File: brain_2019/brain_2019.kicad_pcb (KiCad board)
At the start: 2 copper layers, 54 x 50 mm, 60 parts, among them J1 CocobotCAN, J2 CocobotCAN, J3 JST_PH_S6B-PH-SM4-TB_06x2.00m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, J4 JST_PH_S2B-PH-SM4-TB_02x2.00m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, J5 Conn_01x02, J6 Conn_01x04, J7 JST_PH_S4B-PH-SM4-TB_04x2.00m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, J8 JST_PH_S4B-PH-SM4-TB_04x2.00m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, J9 JST_PH_S2B-PH-SM4-TB_02x2.00m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, U1 MAX3051ESA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

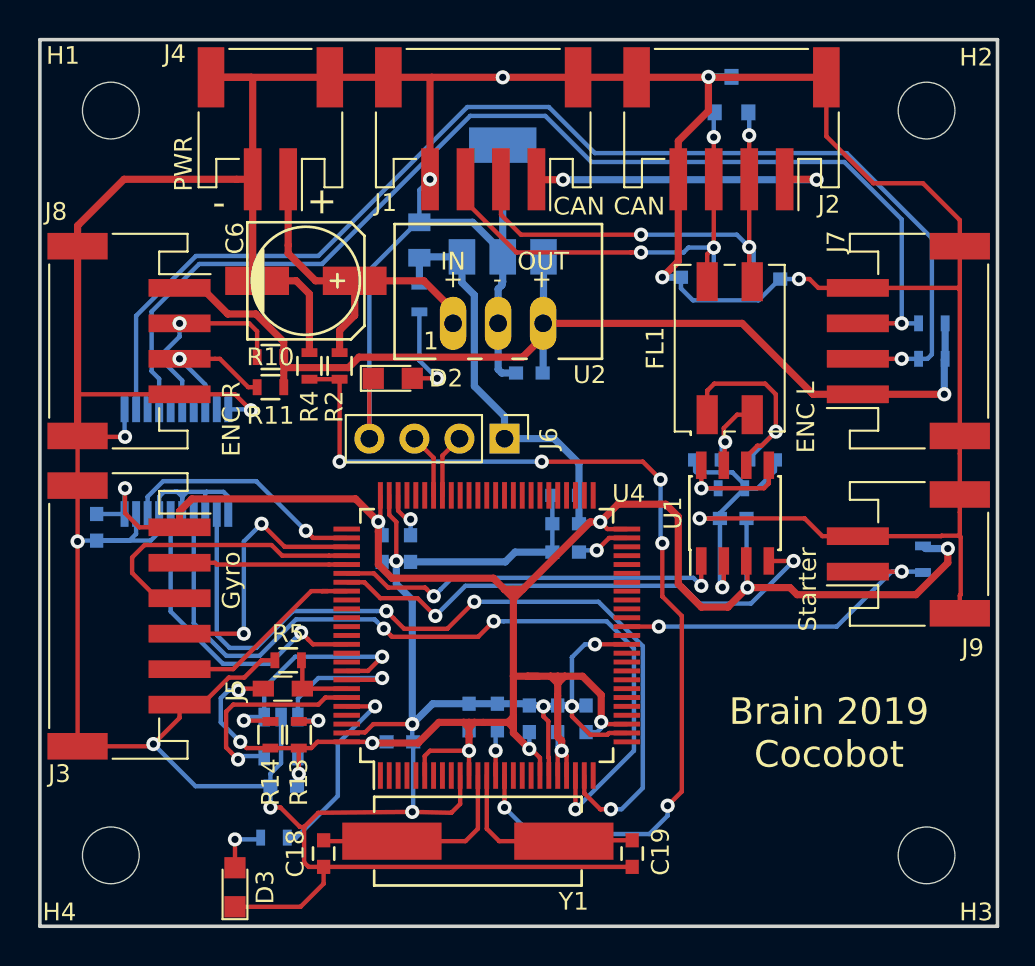
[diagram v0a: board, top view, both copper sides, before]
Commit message: Update brain 2019 with new CAN connector
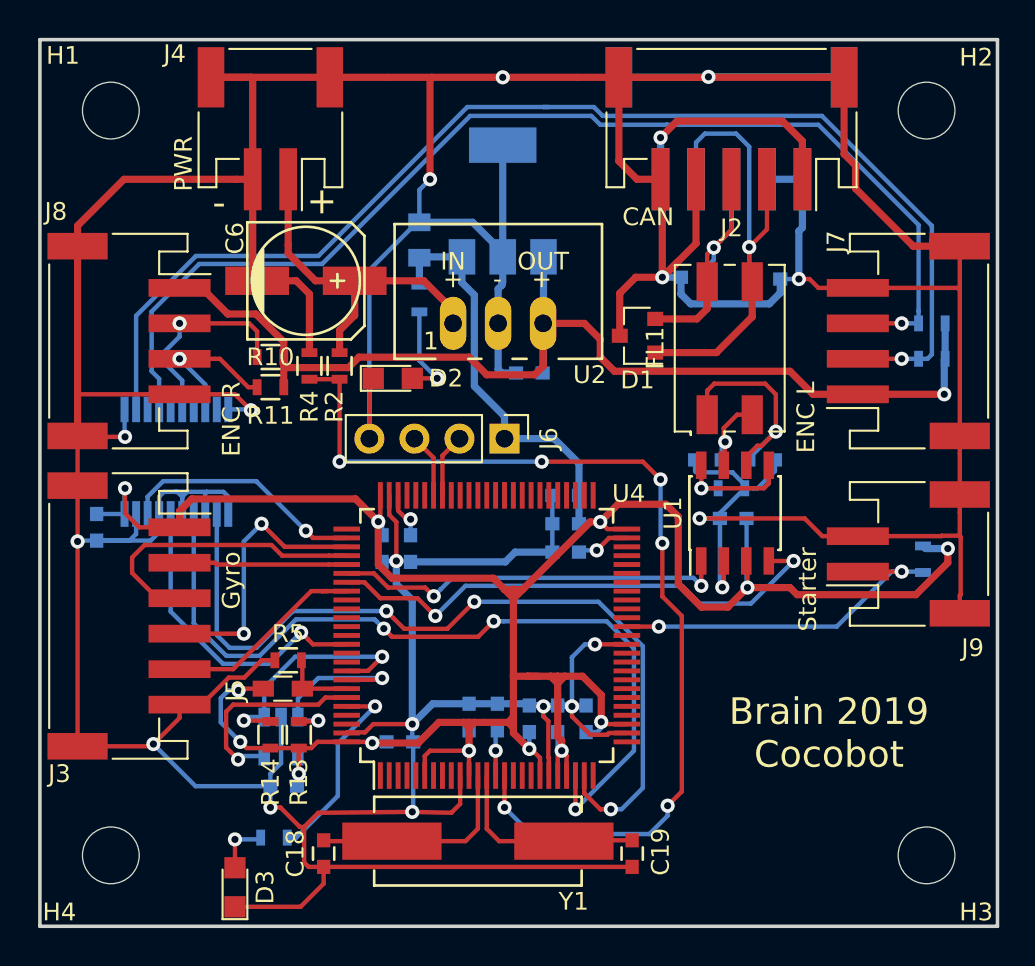
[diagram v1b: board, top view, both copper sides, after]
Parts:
- D1: moved to F.Cu
- J1: footprint espitall:JST_PH_S4B-PH-SM4-TB_04x2.00mm_Angled -> espitall:JST_PH_S5B-PH-SM4-TB_05x2.00mm_Angled; moved to B.Cu
- J2: footprint espitall:JST_PH_S4B-PH-SM4-TB_04x2.00mm_Angled -> espitall:JST_PH_S5B-PH-SM4-TB_05x2.00mm_Angled
- moved D1 14.6 mm to (83.7, 66.7), turned to 180 degrees
- moved J1 14.0 mm to (89.0, 55.0), turned to 0 degrees
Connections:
- H1 pad 1: Net-(H1-Pad1) -> (no net)
- H2 pad 1: Net-(H2-Pad1) -> (no net)
- H3 pad 1: Net-(H3-Pad1) -> (no net)
- H4 pad 1: Net-(H4-Pad1) -> (no net)
- U4 pad 1: Net-(U4-Pad1) -> (no net)
- U4 pad 16: Net-(U4-Pad16) -> (no net)
- U4 pad 17: Net-(U4-Pad17) -> (no net)
- U4 pad 18: Net-(U4-Pad18) -> (no net)
- U4 pad 2: Net-(U4-Pad2) -> (no net)
- U4 pad 25: Net-(U4-Pad25) -> (no net)
- U4 pad 26: Net-(U4-Pad26) -> (no net)
- U4 pad 29: Net-(U4-Pad29) -> (no net)
- U4 pad 3: Net-(U4-Pad3) -> (no net)
- U4 pad 30: Net-(U4-Pad30) -> (no net)
- U4 pad 31: Net-(U4-Pad31) -> (no net)
- U4 pad 32: Net-(U4-Pad32) -> (no net)
- U4 pad 33: Net-(U4-Pad33) -> (no net)
- U4 pad 34: Net-(U4-Pad34) -> (no net)
- U4 pad 35: Net-(U4-Pad35) -> (no net)
- U4 pad 36: Net-(U4-Pad36) -> (no net)
- U4 pad 38: Net-(U4-Pad38) -> (no net)
- U4 pad 4: Net-(U4-Pad4) -> (no net)
- U4 pad 40: Net-(U4-Pad40) -> (no net)
- U4 pad 41: Net-(U4-Pad41) -> (no net)
- U4 pad 42: Net-(U4-Pad42) -> (no net)
- U4 pad 43: Net-(U4-Pad43) -> (no net)
- U4 pad 44: Net-(U4-Pad44) -> (no net)
- U4 pad 45: Net-(U4-Pad45) -> (no net)
- U4 pad 46: Net-(U4-Pad46) -> (no net)
- U4 pad 47: Net-(U4-Pad47) -> (no net)
- U4 pad 48: Net-(U4-Pad48) -> (no net)
- U4 pad 5: Net-(U4-Pad5) -> (no net)
- U4 pad 51: Net-(U4-Pad51) -> (no net)
- U4 pad 52: Net-(U4-Pad52) -> (no net)
- U4 pad 53: Net-(U4-Pad53) -> (no net)
- U4 pad 54: Net-(U4-Pad54) -> (no net)
- U4 pad 55: Net-(U4-Pad55) -> (no net)
- U4 pad 56: Net-(U4-Pad56) -> (no net)
- U4 pad 57: Net-(U4-Pad57) -> (no net)
- U4 pad 58: Net-(U4-Pad58) -> (no net)
- U4 pad 59: Net-(U4-Pad59) -> (no net)
- U4 pad 60: Net-(U4-Pad60) -> (no net)
- U4 pad 61: Net-(U4-Pad61) -> (no net)
- U4 pad 62: Net-(U4-Pad62) -> (no net)
- U4 pad 63: Net-(U4-Pad63) -> (no net)
- U4 pad 64: Net-(U4-Pad64) -> (no net)
- U4 pad 65: Net-(U4-Pad65) -> (no net)
- U4 pad 66: Net-(U4-Pad66) -> (no net)
- U4 pad 67: Net-(U4-Pad67) -> (no net)
- U4 pad 7: Net-(U4-Pad7) -> (no net)
- U4 pad 70: Net-(U4-Pad70) -> (no net)
- U4 pad 71: Net-(U4-Pad71) -> (no net)
- U4 pad 72: Net-(U4-Pad72) -> (no net)
- U4 pad 76: Net-(U4-Pad76) -> (no net)
- U4 pad 8: Net-(U4-Pad8) -> (no net)
- U4 pad 84: Net-(U4-Pad84) -> (no net)
- U4 pad 85: Net-(U4-Pad85) -> (no net)
- U4 pad 86: Net-(U4-Pad86) -> (no net)
- U4 pad 87: Net-(U4-Pad87) -> (no net)
- U4 pad 88: Net-(U4-Pad88) -> (no net)
- U4 pad 9: Net-(U4-Pad9) -> (no net)
- U4 pad 90: Net-(U4-Pad90) -> (no net)
- U4 pad 91: Net-(U4-Pad91) -> (no net)
- U4 pad 97: Net-(U4-Pad97) -> (no net)
- U4 pad 98: Net-(U4-Pad98) -> (no net)
- U5 pad 3: Net-(U5-Pad3) -> (no net)
- U5 pad 5: Net-(U5-Pad5) -> (no net)
- U5 pad 7: Net-(U5-Pad7) -> (no net)
- U5 pad 9: Net-(U5-Pad9) -> (no net)
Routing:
- net GND: track 399.6 -> 433.8 mm
- net Net-(C5-Pad1): track 28.1 -> 17.1 mm, vias 3 -> 1
- net Net-(J1-Pad1): track 17.6 -> 13.4 mm, vias 2 -> 1
- net +5V: track 60.7 -> 63.1 mm
- net /Encoders/enc_l_A_5v: track 68.9 -> 70.1 mm
- net /Encoders/enc_l_B_5v: track 64.3 -> 65.0 mm
- net Net-(C4-Pad1): track 28.3 -> 27.7 mm, vias 3 -> 1
